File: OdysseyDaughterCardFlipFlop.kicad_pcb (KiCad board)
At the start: 2 copper layers, 47.8 x 46.6 mm, 1 part, among them X1 OdysseyDaughterCard

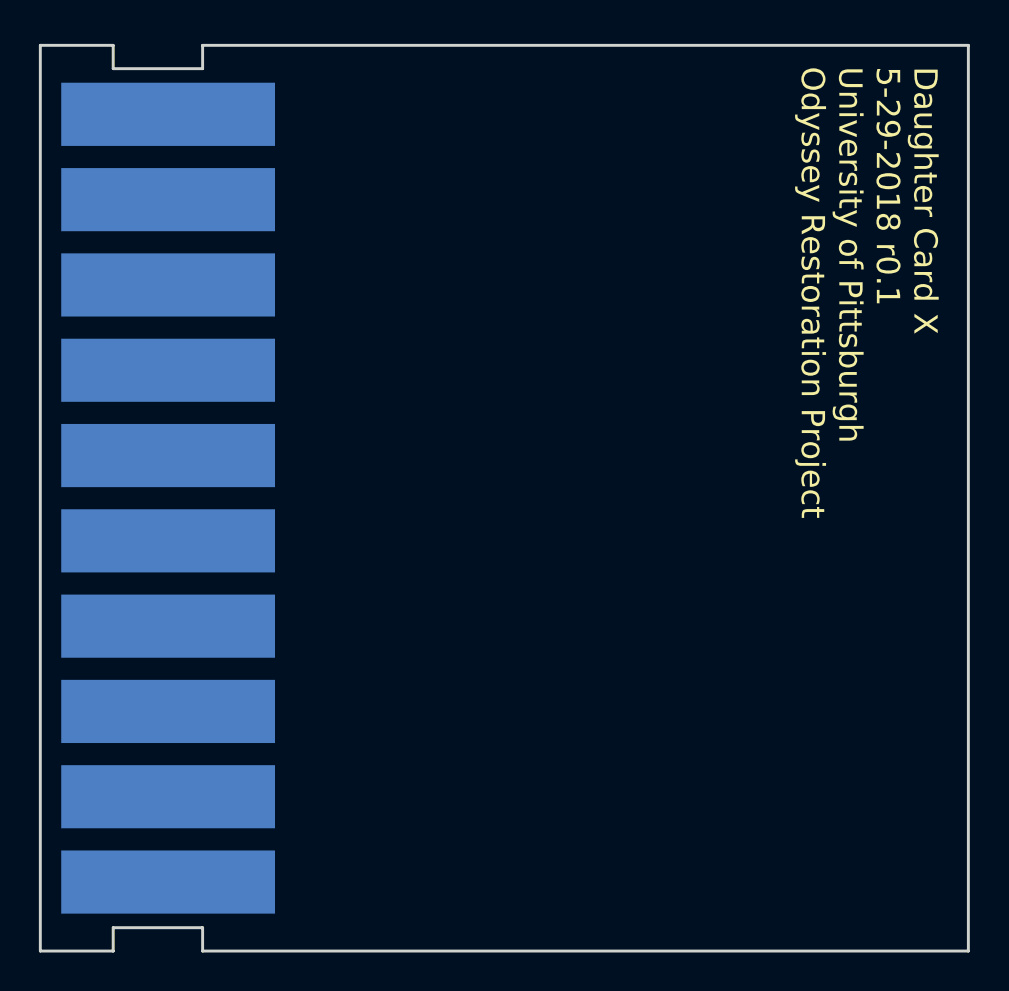
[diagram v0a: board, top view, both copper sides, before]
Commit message: V0.1 of the flip flop daughter card
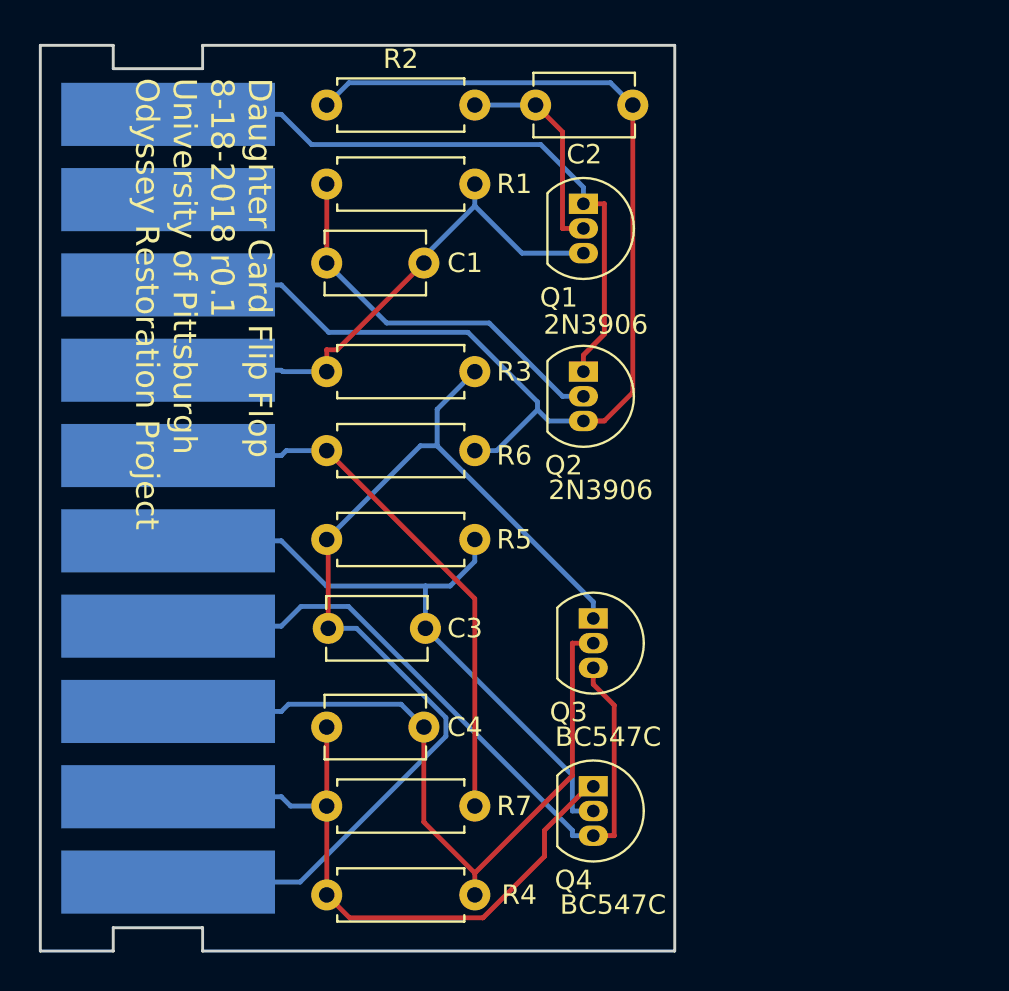
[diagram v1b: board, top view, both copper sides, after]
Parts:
- added C1: 0.1u, Capacitor_THT:C_Disc_D5.1mm_W3.2mm_P5.00mm, F.Cu at (137.2, 88.9)
- added C2: 0.1u, Capacitor_THT:C_Disc_D5.1mm_W3.2mm_P5.00mm, F.Cu at (152.9, 80.8)
- added C3: 100p, Capacitor_THT:C_Disc_D5.1mm_W3.2mm_P5.00mm, F.Cu at (142.2, 107.7)
- added C4: 100p, Capacitor_THT:C_Disc_D5.1mm_W3.2mm_P5.00mm, F.Cu at (137.2, 112.8)
- added Q1: 2N3906, Package_TO_SOT_THT:TO-92_Inline, F.Cu at (150.4, 85.9)
- added Q2: 2N3906, Package_TO_SOT_THT:TO-92_Inline, F.Cu at (150.4, 94.5)
- added Q3: BC547C, Package_TO_SOT_THT:TO-92_Inline, F.Cu at (150.9, 107.2)
- added Q4: BC547C, Package_TO_SOT_THT:TO-92_Inline, F.Cu at (150.9, 115.8)
- added R1: 47k, Resistor_THT:R_Axial_DIN0207_L6.3mm_D2.5mm_P7.62mm_Horizontal, F.Cu at (137.2, 84.8)
- added R2: 47k, Resistor_THT:R_Axial_DIN0207_L6.3mm_D2.5mm_P7.62mm_Horizontal, F.Cu at (137.2, 80.8)
- added R3: 2.2k, Resistor_THT:R_Axial_DIN0207_L6.3mm_D2.5mm_P7.62mm_Horizontal, F.Cu at (144.8, 94.5)
- added R4: 47k, Resistor_THT:R_Axial_DIN0207_L6.3mm_D2.5mm_P7.62mm_Horizontal, F.Cu at (137.2, 121.4)
- added R5: 47k, Resistor_THT:R_Axial_DIN0207_L6.3mm_D2.5mm_P7.62mm_Horizontal, F.Cu at (137.2, 103.1)
- added R6: 1k, Resistor_THT:R_Axial_DIN0207_L6.3mm_D2.5mm_P7.62mm_Horizontal, F.Cu at (137.2, 98.6)
- added R7: 1k, Resistor_THT:R_Axial_DIN0207_L6.3mm_D2.5mm_P7.62mm_Horizontal, F.Cu at (144.8, 116.8)
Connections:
- net Net-(X1-Pad9) renamed /Card9
- X1 pad 1: Net-(X1-Pad1) -> /Card1
- X1 pad 10: Net-(X1-Pad10) -> /Card10
- X1 pad 2: Net-(X1-Pad2) -> /Card2
- X1 pad 3: Net-(X1-Pad3) -> /Card3
- X1 pad 4: Net-(X1-Pad4) -> GND
- X1 pad 5: Net-(X1-Pad5) -> /Card5
- X1 pad 6: Net-(X1-Pad6) -> /Card6
- X1 pad 7: Net-(X1-Pad7) -> /Card7
- X1 pad 8: Net-(X1-Pad8) -> /Card8
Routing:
- net /Card8: track 0.00 -> 63.2 mm
- net /Card1: track 0.00 -> 55.4 mm
- net /Card3: track 0.00 -> 38.5 mm
- net GND: track 0.00 -> 37.5 mm
- net /Card2: track 0.00 -> 34.8 mm
- net /Card5: track 0.00 -> 34.2 mm
- net /Card10: track 0.00 -> 33.9 mm
- net /Card6: track 0.00 -> 29.7 mm
- net /Card7: track 0.00 -> 27.9 mm
- net Net-(C1-Pad1): track 0.00 -> 20.1 mm
- net Net-(C2-Pad2): track 0.00 -> 11.1 mm
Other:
- board size 47.8 x 46.6 mm -> 32.6 x 46.6 mm
- board text added: "Daughter Card Flip Flop 8-18-2018 r0.1 University of Pittsburgh Odyssey Restoration Project"
- board text removed: "Daughter Card X 5-29-2018 r0.1 University of Pittsburgh Odyssey Restoration Project"
